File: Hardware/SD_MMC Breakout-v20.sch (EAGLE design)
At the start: 7 parts, among them U1 SD_CARD_SOCKET

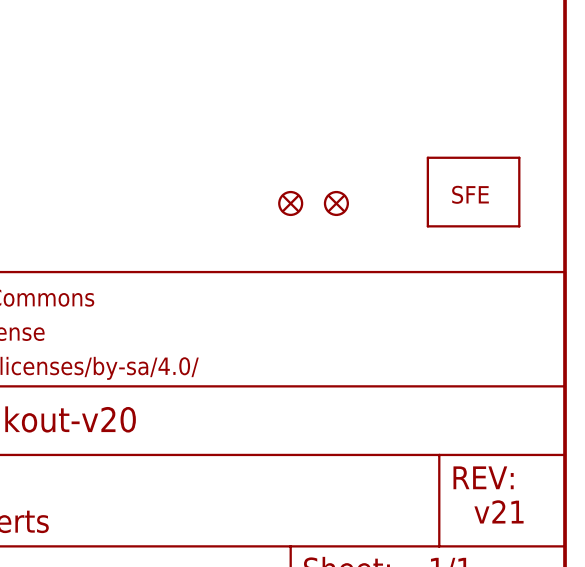
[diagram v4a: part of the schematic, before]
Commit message: changed fiducial to regular size
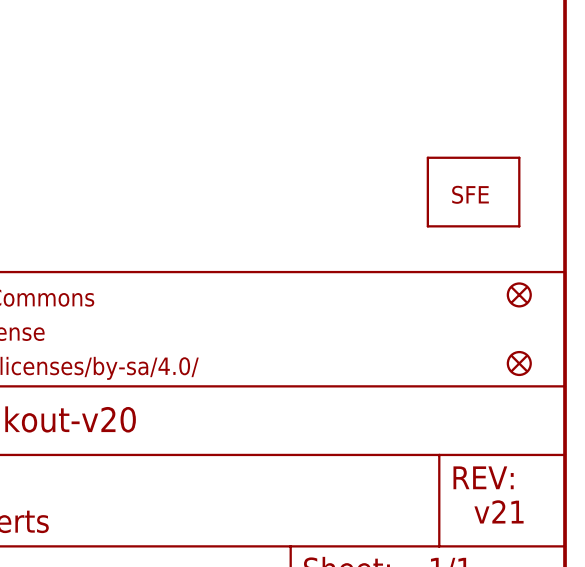
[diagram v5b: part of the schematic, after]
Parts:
- removed JP2, JP3: FIDUCIALUFIDUCIAL, SparkFun:FIDUCIALUFIDUCIAL
- added FID1, FID2: FIDUCIAL1X2, SparkFun-Aesthetics:FIDUCIAL1X2
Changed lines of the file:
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@@
 <?xml version="1.0" encoding="utf-8"?>
 <!DOCTYPE eagle SYSTEM "eagle.dtd">
-<eagle version="6.4">
+<eagle version="6.5.0">
 <drawing>
 <settings>
@@
 <part name="U$3" library="SparkFun-Aesthetics" deviceset="OSHW-LOGO" device="S"/>
 <part name="JP5" library="SparkFun-Connectors" deviceset="M10" device="&quot;"/>
-<part name="JP2" library="SparkFun" deviceset="FIDUCIAL" device="UFIDUCIAL"/>
-<part name="JP3" library="SparkFun" deviceset="FIDUCIAL" device="UFIDUCIAL"/>
+<part name="FID1" library="SparkFun-Aesthetics" deviceset="FIDUCIAL" device="1X2"/>
+<part name="FID2" library="SparkFun-Aesthetics" deviceset="FIDUCIAL" device="1X2"/>
 </parts>
 <sheets>
@@
 <instance part="U$3" gate="G$1" x="132.08" y="10.16"/>
 <instance part="JP5" gate="G$1" x="93.98" y="116.84"/>
-<instance part="JP2" gate="G$1" x="218.44" y="43.18"/>
-<instance part="JP3" gate="G$1" x="223.52" y="43.18"/>
+<instance part="FID1" gate="G$1" x="243.84" y="33.02"/>
+<instance part="FID2" gate="G$1" x="243.84" y="25.4"/>
 </instances>
 <busses>
